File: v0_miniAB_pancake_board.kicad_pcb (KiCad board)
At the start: 2 copper layers, 51 x 38.3 mm, 17 parts, among them J1 A+ A- B+ B-, J10 , J11 , J12 , J13 BLTOUCH, J2 , J3 , J4 , J5 , J6 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

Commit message: Silkscreen change and gerber uploads
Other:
- board text added: "24V HEAT_GND TH0 TH1 PROBE FAN1 SERVO 5V"
- board text added: "A+ A- B+ B- X END FAN0 LED GND"
- board text added: "JLCJLCJLCJLC"
- board text removed: "24V HEAT_GND TH0 TH1 SW0 FAN1 SERVO 5V"
- board text removed: "A+ A- B+ B- SW1 FAN0 LED GND"
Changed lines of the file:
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@@
       (plotinvisibletext false)
       (sketchpadsonfab false)
-      (subtractmaskfromsilk false)
+      (subtractmaskfromsilk true)
       (outputformat 1)
       (mirror false)
@@
     (fp_line (start -3.325 0.98) (end -3.325 -7.92) (layer "F.Fab") (width 0.1))
     (pad "" np_thru_hole circle (at 1.5 -4.32 150) (size 3 3) (drill 3) (layers *.Cu *.Mask))
-    (pad "1" thru_hole roundrect (at 0 0 150) (size 1.5 2.02) (drill 1.02) (layers *.Cu *.Mask) (roundrect_rratio 0.166667)
+    (pad "1" thru_hole roundrect (at 0 0 150) (size 1.5 2.02) (drill 1.02) (layers *.Cu *.Mask) (roundrect_rratio 0.1666673333)
       (net 13 "/heat_gnd") (pinfunction "Pin_1") (pintype "passive"))
     (pad "2" thru_hole oval (at 3 0 150) (size 1.5 2.02) (drill 1.02) (layers *.Cu *.Mask)
@@
     (fp_line (start -1.11 -2.11) (end -2.36 -2.11) (layer "F.Fab") (width 0.1))
     (fp_line (start -1.95 -1.7) (end -1.95 2.8) (layer "F.Fab") (width 0.1))
-    (pad "1" thru_hole roundrect (at 0 0 180) (size 1.2 1.75) (drill 0.75) (layers *.Cu *.Mask) (roundrect_rratio 0.208333)
+    (pad "1" thru_hole roundrect (at 0 0 180) (size 1.2 1.75) (drill 0.75) (layers *.Cu *.Mask) (roundrect_rratio 0.2083333333)
       (net 8 "+5V") (pinfunction "Pin_1") (pintype "passive"))
     (pad "2" thru_hole oval (at 2 0 180) (size 1.2 1.75) (drill 0.75) (layers *.Cu *.Mask)
@@
     (fp_line (start -1.95 2.8) (end 5.95 2.8) (layer "F.Fab") (width 0.1))
     (fp_line (start -2.36 -2.11) (end -2.36 -0.86) (layer "F.Fab") (width 0.1))
-    (pad "1" thru_hole roundrect (at 0 0 35) (size 1.2 1.75) (drill 0.75) (layers *.Cu *.Mask) (roundrect_rratio 0.208333)
+    (pad "1" thru_hole roundrect (at 0 0 35) (size 1.2 1.75) (drill 0.75) (layers *.Cu *.Mask) (roundrect_rratio 0.2083333333)
       (net 8 "+5V") (pinfunction "Pin_1") (pintype "passive"))
     (pad "2" thru_hole oval (at 2 0 35) (size 1.2 1.75) (drill 0.75) (layers *.Cu *.Mask)
@@
     (pad "" np_thru_hole circle (at 18.86 -4.32) (size 3 3) (drill 3) (layers *.Cu *.Mask))
     (pad "" np_thru_hole circle (at 2.16 -4.32) (size 3 3) (drill 3) (layers *.Cu *.Mask))
-    (pad "1" thru_hole roundrect (at 0 0) (size 1.5 1.5) (drill 1.02) (layers *.Cu *.Mask) (roundrect_rratio 0.166667)
+    (pad "1" thru_hole roundrect (at 0 0) (size 1.5 1.5) (drill 1.02) (layers *.Cu *.Mask) (roundrect_rratio 0.1666673333)
       (net 4 "/A+") (pinfunction "Pin_1") (pintype "passive"))
     (pad "2" thru_hole circle (at 3 0) (size 1.5 1.5) (drill 1.02) (layers *.Cu *.Mask)
@@
     (effects (font (size 2 2) (thickness 0.3)) (justify mirror))
   )
-  (gr_text "A+\n\nA-\n\nB+\n\nB-\n\nSW1\n\nFAN0\n\nLED\n\nGND" (at 102.3112 93.8276 90) (layer "B.SilkS")
+  (gr_text "A+\n\nA-\n\nB+\n\nB-\n\nX END\n\nFAN0\n\nLED\n\nGND" (at 102.3112 93.8276 90) (layer "B.SilkS")
     (effects (font (size 1 1) (thickness 0.15)) (justify left mirror))
   )
-  (gr_text "24V\n\nHEAT_GND\n\nTH0\n\nTH1\n\nSW0\n\nFAN1\n\nSERVO\n\n5V" (at 101.7016 100.584 90) (layer "B.SilkS")
+  (gr_text "24V\n\nHEAT_GND\n\nTH0\n\nTH1\n\nPROBE\n\nFAN1\n\nSERVO\n\n5V" (at 101.7016 100.584 90) (layer "B.SilkS")
     (effects (font (size 1 1) (thickness 0.15)) (justify left mirror))
   )
@@
     (effects (font (size 1 1) (thickness 0.15)))
   )
+  (gr_text "JLCJLCJLCJLC" (at 118.6688 93.9292 -33) (layer "F.SilkS")
+    (effects (font (size 0.9 0.7) (thickness 0.1)))
+  )
   (gr_text "fork by: matthew & @famichu\n2022" (at 100.9396 91.3892) (layer "F.SilkS")
     (effects (font (size 1 1) (thickness 0.15)))
@@
   (segment (start 87.7316 83.2104) (end 85.7504 83.2104) (width 0.8) (layer "F.Cu") (net 1))
   (segment (start 99.4396 94.9184) (end 87.7316 83.2104) (width 0.8) (layer "F.Cu") (net 1))
-  (segment (start 85.7504 83.2104) (end 85.598 83.058) (width 0.8) (layer "F.Cu") (net 1))
   (segment (start 99.4396 96.9714) (end 99.4396 94.9184) (width 0.8) (layer "F.Cu") (net 1))
   (segment (start 96.4396 96.9714) (end 96.4396 93.451517) (width 0.8) (layer "F.Cu") (net 2))
@@
   (segment (start 85.009984 85.3948) (end 84.239798 84.624614) (width 0.8) (layer "F.Cu") (net 2))
   (segment (start 93.4396 96.9714) (end 82.825585 86.357385) (width 0.8) (layer "F.Cu") (net 3))
-  (segment (start 82.825585 85.942439) (end 82.769573 85.886427) (width 0.8) (layer "F.Cu") (net 3))
   (segment (start 82.825585 86.357385) (end 82.825585 85.942439) (width 0.8) (layer "F.Cu") (net 3))
-  (segment (start 81.355359 87.300641) (end 81.355359 87.397029) (width 0.8) (layer "F.Cu") (net 4))
   (segment (start 81.355359 87.397029) (end 90.4396 96.48127) (width 0.8) (layer "F.Cu") (net 4))
   (segment (start 90.4396 96.48127) (end 90.4396 96.9714) (width 0.8) (layer "F.Cu") (net 4))
@@
   (segment (start 106.8678 98.3996) (end 105.4396 96.9714) (width 0.78) (layer "F.Cu") (net 7))
   (segment (start 108.762156 98.3996) (end 106.8678 98.3996) (width 0.78) (layer "F.Cu") (net 7))
-  (segment (start 122.801388 107.3912) (end 122.5296 107.3912) (width 0.78) (layer "F.Cu") (net 7))
   (segment (start 109.779111 99.416555) (end 108.762156 98.3996) (width 0.78) (layer "F.Cu") (net 7))
   (segment (start 122.5296 107.3912) (end 120.122436 104.984036) (width 0.78) (layer "F.Cu") (net 7))
@@
   (segment (start 117.2464 106.3244) (end 111.7926 106.3244) (width 0.78) (layer "F.Cu") (net 9))
   (segment (start 111.7926 106.3244) (end 105.4396 99.9714) (width 0.78) (layer "F.Cu") (net 9))
-  (segment (start 117.2972 106.3752) (end 117.2464 106.3244) (width 0.78) (layer "F.Cu") (net 9))
   (via (at 86.36 87.4776) (size 0.8) (drill 0.4) (layers "F.Cu" "B.Cu") (free) (net 10))
   (via (at 88.7984 109.1692) (size 0.8) (drill 0.4) (layers "F.Cu" "B.Cu") (free) (net 10))
@@
   (segment (start 102.4636 114.7252) (end 103.1386 115.4002) (width 0.78) (layer "F.Cu") (net 16))
   (segment (start 109.2882 115.4002) (end 116.394384 108.294016) (width 0.78) (layer "F.Cu") (net 16))
-  (segment (start 116.828416 108.294016) (end 116.8908 108.3564) (width 0.78) (layer "F.Cu") (net 16))
   (segment (start 110.6424 112.7252) (end 108.8136 112.7252) (width 0.25) (layer "F.Cu") (net 17))
   (segment (start 108.718667 112.630267) (end 108.396533 112.630267) (width 0.25) (layer "F.Cu") (net 17))

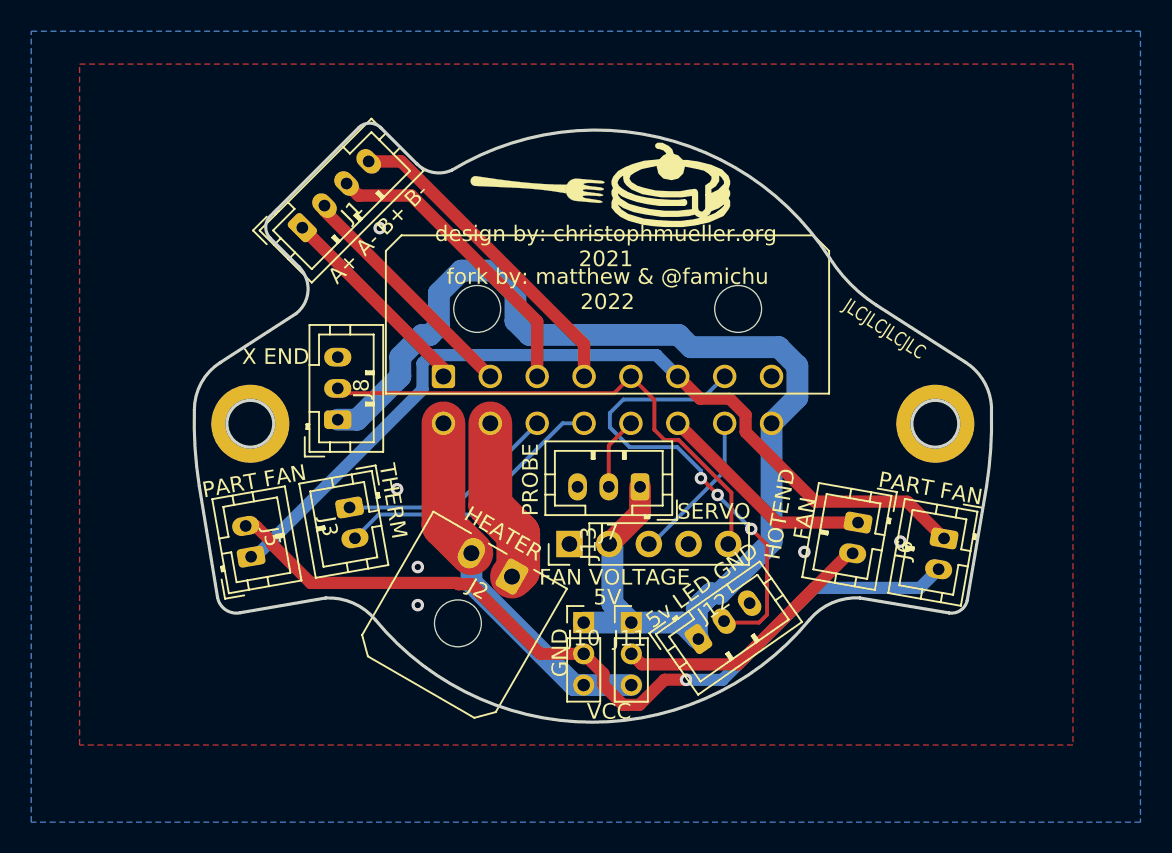
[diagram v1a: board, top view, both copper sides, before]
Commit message: Fix connectors direction and organize routes
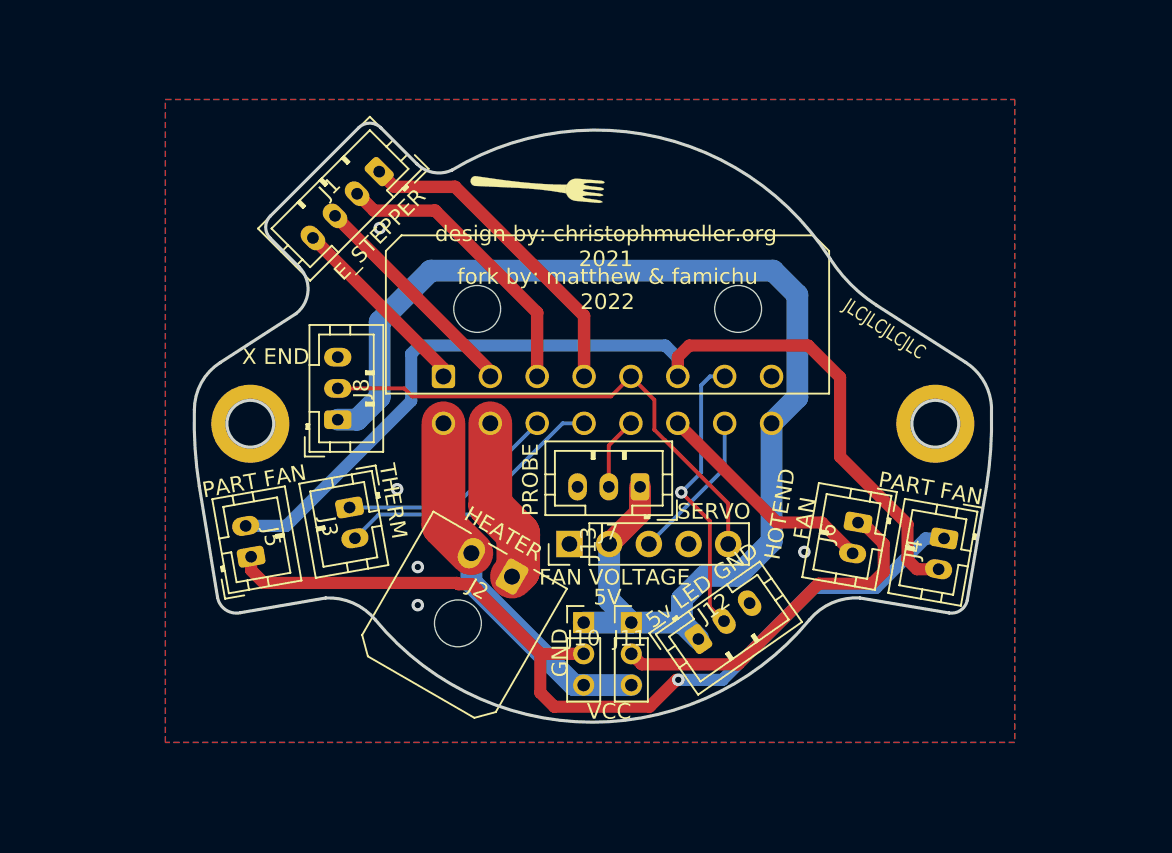
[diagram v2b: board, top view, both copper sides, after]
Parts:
- removed REF** (x2): pancake, v0_pancake_board:pancake
- H1, H2: value (none) -> MountingHole_Pad
- J1: value A+ A- B+ B- -> E_STEPPER
- J10: value (none) -> FAN0_V_JUMPER
- J11: value (none) -> FAN1_V_JUMPER
- J12: value (none) -> RGB LED
- J2: value (none) -> HEATER
- J3: value (none) -> THERM
- J4, J5: value (none) -> PART FAN
- J6: value (none) -> HOTEND FAN
- J8: value (none) -> ENDSTOP1
- moved J1 6.09 mm to (86.3, 83.9), turned to -135 degrees
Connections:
- J1 pad 1: /A+ -> /B-
- J1 pad 2: /A- -> /B+
- J1 pad 3: /B+ -> /A-
- J1 pad 4: /B- -> /A+
- J4 pad 1: /fan0 -> /VFAN0
- J4 pad 2: /VFAN0 -> /fan0
- J5 pad 1: /fan0 -> /VFAN0
- J5 pad 2: /VFAN0 -> /fan0
- J6 pad 1: /fan1 -> /VFAN1
- J6 pad 2: /VFAN1 -> /fan1
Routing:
- net /led: track 30.2 -> 18.5 mm, vias 3 -> 1
- net /fan0: track 56.3 -> 64.2 mm
- net /VFAN1: track 17.6 -> 22.9 mm
- net /VFAN0: track 53.2 -> 57.6 mm
- net +5V: track 77.8 -> 79.9 mm
- net /A-: track 15.4 -> 14.4 mm
- net /A+: track 13.3 -> 12.3 mm
- net /B+: track 19.4 -> 18.8 mm
- net GND: vias 6 -> 5
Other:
- board text added: "fork by: matthew & famichu 2022"
- board text removed: "fork by: matthew & @famichu 2022"
